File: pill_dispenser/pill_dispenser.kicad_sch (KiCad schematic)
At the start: 54 parts, among them J1 Servo, J2 ADC Pins, J3 USB Data, J4 Button Interface, J5 Power, J6 Release Button, J7 5V GPIO, J8 GPIO Pins, Q1 2N3904, Q2 2N3904, SW1 SW_Push, U1 RP2040, U2 W25Q128JVS, U3 LSF0108PW, U4 DS1307Z+, U5 TSDP341xx, Y1 Crystal_ABM8, Y2 32.768 kHz

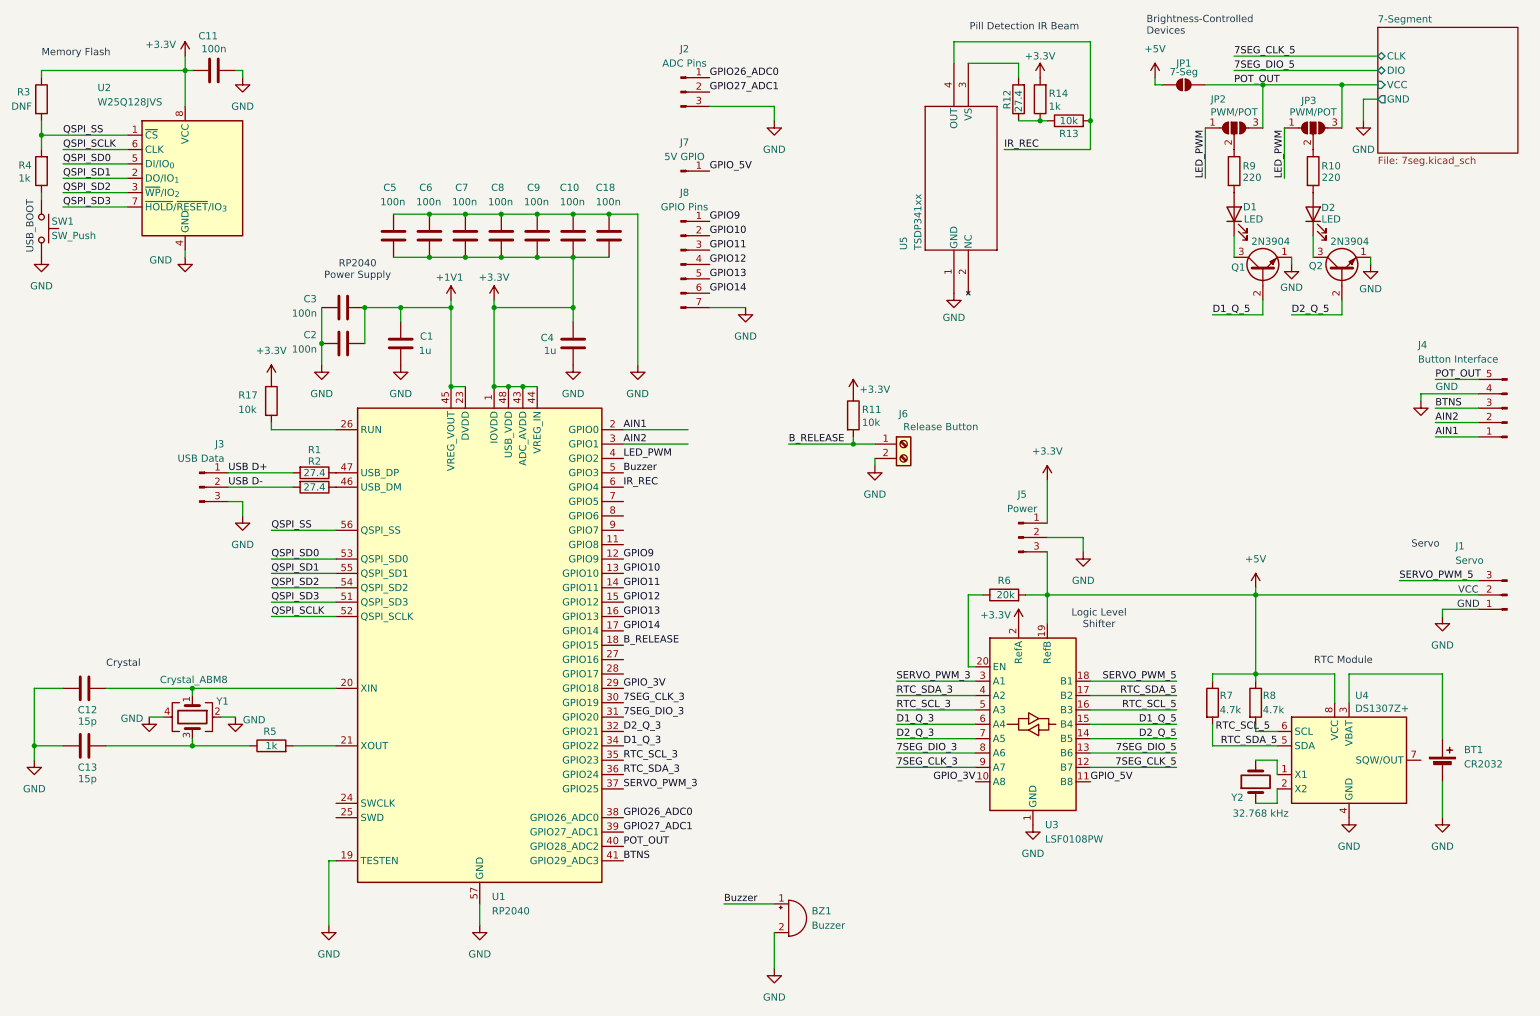
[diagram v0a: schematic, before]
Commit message: update schematics per suggestions
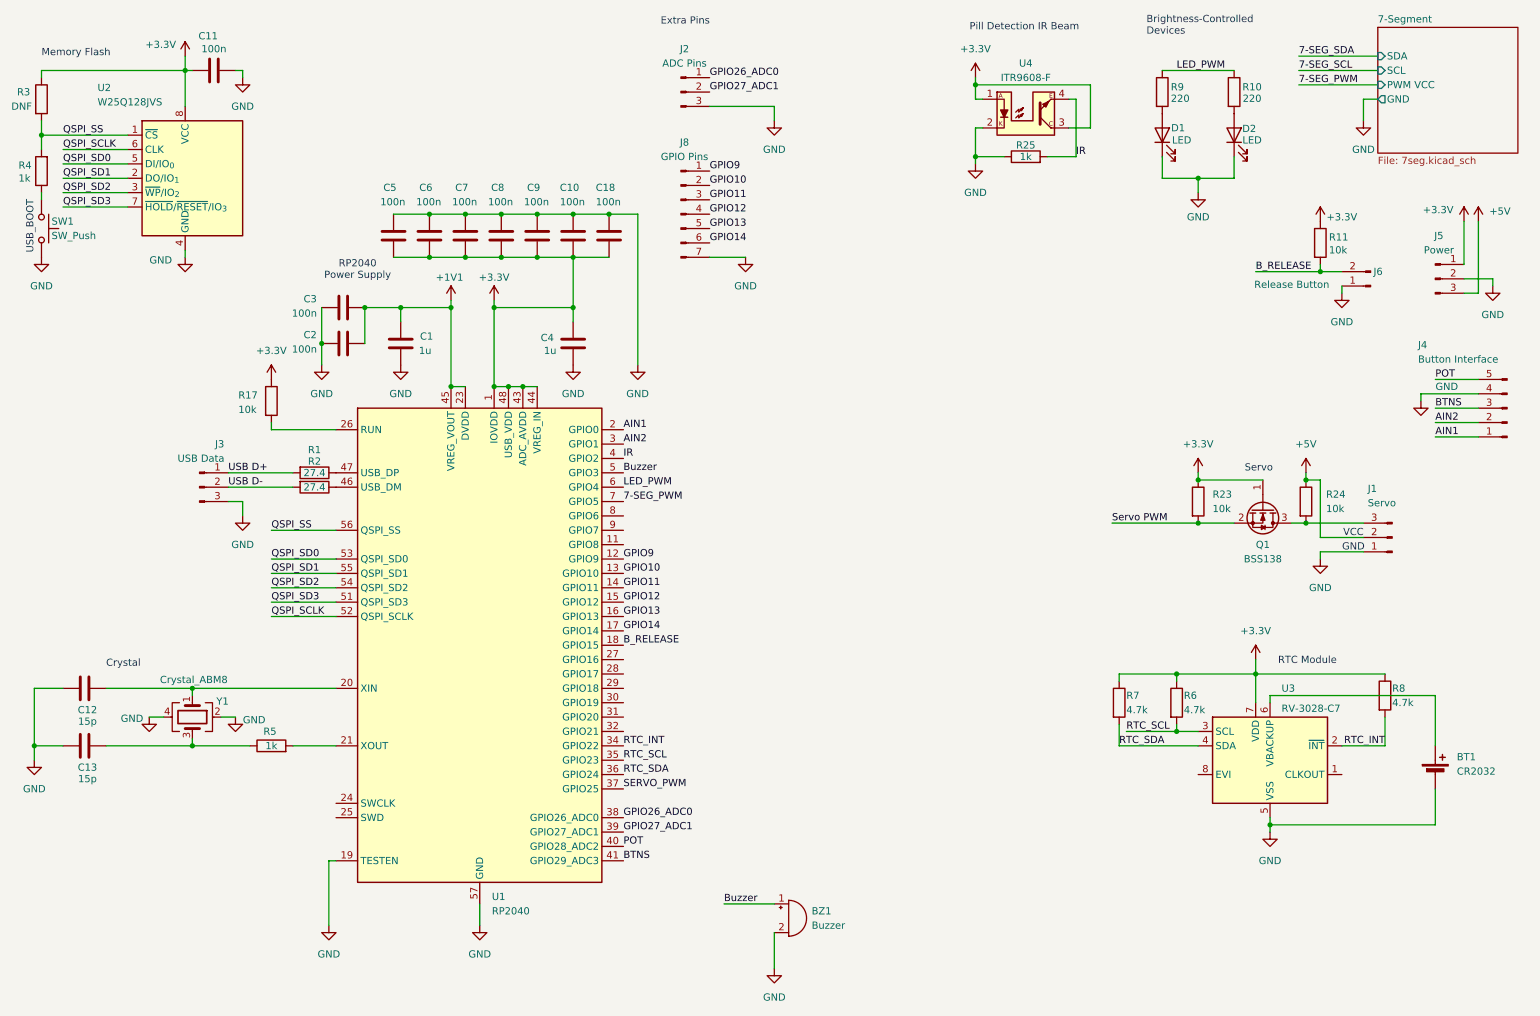
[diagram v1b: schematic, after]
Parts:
- removed J6: Release Button, TerminalBlock_Wuerth:Wuerth_691311400102_P7.62mm, symbol Connector:Screw_Terminal_01x02
- removed J7: 5V GPIO, Connector_PinHeader_2.54mm:PinHeader_1x01_P2.54mm_Vertical, symbol Connector:Conn_01x01_Pin
- removed JP1: 7-Seg, Jumper:SolderJumper-2_P1.3mm_Open_RoundedPad1.0x1.5mm, symbol Jumper:SolderJumper_2_Open
- removed JP2, JP3: PWM/POT, Jumper:SolderJumper-3_P1.3mm_Open_RoundedPad1.0x1.5mm_NumberLabels, symbol Jumper:SolderJumper_3_Open
- removed Q1, Q2: 2N3904, Package_TO_SOT_THT:TO-92_Inline, symbol Transistor_BJT:2N3904
- removed R12: 27.4, Resistor_SMD:R_0402_1005Metric, symbol Device:R
- removed R13: 10k, Resistor_SMD:R_0805_2012Metric, symbol Device:R
- removed R14: 1k, Resistor_SMD:R_0603_1608Metric, symbol Device:R
- removed U3: LSF0108PW, Package_SO:TSSOP-20_4.4x6.5mm_P0.65mm, symbol Logic_LevelTranslator:LSF0108PW
- removed U4: DS1307Z+, Package_SO:SOIC-8_3.9x4.9mm_P1.27mm, symbol Timer_RTC:DS1307Z+
- removed U5: TSDP341xx, footprints:SMD4_TSSP60_VIS, symbol 2025-12-15_03-19-57:TSSP6038TT
- removed Y2: 32.768 kHz, Crystal:Crystal_SMD_EuroQuartz_EQ161-2Pin_3.2x1.5mm, symbol Device:Crystal
- added J6: Release Button, symbol Connector:Conn_01x02_Pin
- added Q1: BSS138, Package_TO_SOT_SMD:SOT-23, symbol Transistor_FET:BSS138
- added R23, R24: 10k, Resistor_SMD:R_0805_2012Metric, symbol Device:R
- added R25: 1k, symbol Device:R
- added U3: RV-3028-C7, Package_SON:MicroCrystal_C7_SON-8_1.5x3.2mm_P0.9mm, symbol Timer_RTC:RV-3028-C7
- added U4: ITR9608-F, OptoDevice:Everlight_ITR9608-F, symbol Sensor_Proximity:ITR9608-F
- R6: value 20k -> 4.7k
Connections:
- net IR_REC is gone; now on net LED_PWM: U1.6 (GPIO4)
- net RTC_SCL_5 is gone; now on net RTC_INT: R8.2
- net RTC_SDA_5 is gone; now on net RTC_SDA: R7.2
- net +3.3V: now also R6.1, R7.1, R8.1, Q1.1 (G), R23.1, U3.7 (VDD), U4.1, U4.3
- net +5V: now also R24.1; no longer R6.2, R7.1, R8.1
- net B_RELEASE: now also J6.2 (Pin_2)
- net GND: now also D1.1 (K), D2.1 (K), J6.1 (Pin_1), R25.1, U3.5 (VSS), U4.2
- net LED_PWM: now also R10.1, R9.1; no longer U1.4 (GPIO2)
- net at BT1.1 (+): now also U3.6 (VBACKUP)
- net 7-SEG_PWM: now reaches U1.7 (GPIO5)
- net 7SEG_CLK_3: no longer names the net of U1.30 (GPIO19)
- net 7SEG_DIO_3: no longer names the net of U1.31 (GPIO20)
- net D1_Q_3 renamed RTC_INT
- net RTC_INT: now also U3.2 (~{INT})
- net D2_Q_3: no longer names the net of U1.32 (GPIO21)
- net GPIO_3V: no longer names the net of U1.29 (GPIO18)
- net POT_OUT renamed POT
- net RTC_SCL_3 renamed RTC_SCL
- net RTC_SCL: now also R6.2, U3.3 (SCL)
- net RTC_SDA_3 renamed RTC_SDA
- net RTC_SDA: now also U3.4 (SDA)
- net SERVO_PWM_3 renamed SERVO_PWM
- net SERVO_PWM_5: no longer names the net of J1.3 (Pin_3)
- net SERVO_PWM_5: now also Q1.3 (D), R24.2
- new net IR: R25.2, U1.4 (GPIO2), U4.4
- new net Servo PWM: Q1.2 (S), R23.2
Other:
- sheet 7-Segment ports: added PWM VCC, SCL, SDA; removed CLK, DIO, VCC
- note added: "Extra Pins"
- note removed: "Logic Level Shifter"
- moved on the sheet: BT1, D1, D2, J1, J5, J8, R10, R11, R7, R9
